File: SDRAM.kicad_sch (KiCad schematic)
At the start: 24 parts, among them J1 Micro_SD_Card_Det_Hirose_DM3AT, U1 W25Q128JVS, U2 IS42S16160J-7TL, U5 W25N01GVZEIG, U7 CAT24C128

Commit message: Looks like FPC should be changed to XF2M-4015-1A
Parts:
- C1, C18, C2, C20, C21, C22, C29, C3, C36, C37, C38: JLCPCB Part # (none) -> C307331
- J1: JLCPCB Part # (none) -> C114218
- R1, R10, R2, R7, R8, R9: JLCPCB Part # (none) -> C25744
- R5, R6: JLCPCB Part # (none) -> C25879
- U2: JLCPCB Part # (none) -> C412833
- U7: JLCPCB Part # (none) -> C6482
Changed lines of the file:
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@@
 			)
 		)
+		(property "JLCPCB Part #" "C307331"
+			(at 224.79 46.99 0)
+			(effects
+				(font
+					(size 1.27 1.27)
+				)
+				(hide yes)
+			)
+		)
 		(pin "1"
 		)
@@
 			)
 		)
+		(property "JLCPCB Part #" "C307331"
+			(at 265.43 46.99 0)
+			(effects
+				(font
+					(size 1.27 1.27)
+				)
+				(hide yes)
+			)
+		)
 		(pin "1"
 		)
@@
 			)
 		)
+		(property "JLCPCB Part #" "C6482"
+			(at 146.05 54.61 0)
+			(effects
+				(font
+					(size 1.27 1.27)
+				)
+				(hide yes)
+			)
+		)
 		(pin "6"
 		)
@@
 			)
 		)
+		(property "JLCPCB Part #" "C25879"
+			(at 161.29 48.26 0)
+			(effects
+				(font
+					(size 1.27 1.27)
+				)
+				(hide yes)
+			)
+		)
 		(pin "1"
 		)
@@
 			)
 		)
+		(property "JLCPCB Part #" "C307331"
+			(at 99.06 50.8 0)
+			(effects
+				(font
+					(size 1.27 1.27)
+				)
+				(hide yes)
+			)
+		)
 		(pin "1"
 		)
@@
 			)
 		)
+		(property "JLCPCB Part #" "C307331"
+			(at 245.11 46.99 0)
+			(effects
+				(font
+					(size 1.27 1.27)
+				)
+				(hide yes)
+			)
+		)
 		(pin "1"
 		)
@@
 			)
 		)
+		(property "JLCPCB Part #" "C25744"
+			(at 34.29 69.85 0)
+			(effects
+				(font
+					(size 1.27 1.27)
+				)
+				(hide yes)
+			)
+		)
 		(pin "1"
 		)
@@
 			)
 		)
+		(property "JLCPCB Part #" "C25744"
+			(at 34.29 38.1 0)
+			(effects
+				(font
+					(size 1.27 1.27)
+				)
+				(hide yes)
+			)
+		)
 		(pin "1"
 		)
@@
 			)
 		)
+		(property "JLCPCB Part #" "C307331"
+			(at 149.86 137.16 0)
+			(effects
+				(font
+					(size 1.27 1.27)
+				)
+				(hide yes)
+			)
+		)
 		(pin "1"
 		)
@@
 			)
 		)
+		(property "JLCPCB Part #" "C307331"
+			(at 255.27 46.99 0)
+			(effects
+				(font
+					(size 1.27 1.27)
+				)
+				(hide yes)
+			)
+		)
 		(pin "1"
 		)
@@
 			)
 		)
+		(property "JLCPCB Part #" "C307331"
+			(at 125.73 53.34 0)
+			(effects
+				(font
+					(size 1.27 1.27)
+				)
+				(hide yes)
+			)
+		)
 		(pin "1"
 		)
@@
 			)
 		)
+		(property "JLCPCB Part #" "C25744"
+			(at 25.4 38.1 0)
+			(effects
+				(font
+					(size 1.27 1.27)
+				)
+				(hide yes)
+			)
+		)
 		(pin "1"
 		)
@@
 			)
 		)
+		(property "JLCPCB Part #" "C307331"
+			(at 214.63 46.99 0)
+			(effects
+				(font
+					(size 1.27 1.27)
+				)
+				(hide yes)
+			)
+		)
 		(pin "1"
 		)
@@
 			)
 		)
+		(property "JLCPCB Part #" "C114218"
+			(at 73.66 53.34 0)
+			(effects
+				(font
+					(size 1.27 1.27)
+				)
+				(hide yes)
+			)
+		)
 		(pin "9"
 		)
@@
 			)
 		)
+		(property "JLCPCB Part #" "C307331"
+			(at 234.95 46.99 0)
+			(effects
+				(font
+					(size 1.27 1.27)
+				)
+				(hide yes)
+			)
+		)
 		(pin "1"
 		)
@@
 			)
 		)
+		(property "JLCPCB Part #" "C412833"
+			(at 240.03 104.14 0)
+			(effects
+				(font
+					(size 1.27 1.27)
+				)
+				(hide yes)
+			)
+		)
 		(pin "48"
 		)
@@
 			)
 		)
+		(property "JLCPCB Part #" "C25744"
+			(at 16.51 38.1 0)
+			(effects
+				(font
+					(size 1.27 1.27)
+				)
+				(hide yes)
+			)
+		)
 		(pin "1"
 		)
@@
 			)
 		)
+		(property "JLCPCB Part #" "C25744"
+			(at 128.27 137.16 0)
+			(effects
+				(font
+					(size 1.27 1.27)
+				)
+				(hide yes)
+			)
+		)
 		(pin "2"
 		)
@@
 			)
 		)
+		(property "JLCPCB Part #" "C25744"
+			(at 46.99 135.89 0)
+			(effects
+				(font
+					(size 1.27 1.27)
+				)
+				(hide yes)
+			)
+		)
 		(pin "2"
 		)
@@
 			)
 		)
+		(property "JLCPCB Part #" "C307331"
+			(at 68.58 135.89 0)
+			(effects
+				(font
+					(size 1.27 1.27)
+				)
+				(hide yes)
+			)
+		)
 		(pin "1"
 		)
@@
 			)
 		)
+		(property "JLCPCB Part #" "C25879"
+			(at 168.91 48.26 0)
+			(effects
+				(font
+					(size 1.27 1.27)
+				)
+				(hide yes)
+			)
+		)
 		(pin "1"
 		)
@@
 			)
 		)
+		(property "JLCPCB Part #" ""
+			(at 139.7 151.13 0)
+			(effects
+				(font
+					(size 1.27 1.27)
+				)
+				(hide yes)
+			)
+		)
 		(pin "8"
 		)
@@
 			)
 		)
+		(property "JLCPCB Part #" ""
+			(at 58.42 149.86 0)
+			(effects
+				(font
+					(size 1.27 1.27)
+				)
+				(hide yes)
+			)
+		)
 		(pin "8"
 		)
@@
 			(at 204.47 46.99 0)
 			(effects
+				(font
+					(size 1.27 1.27)
+				)
+				(hide yes)
+			)
+		)
+		(property "JLCPCB Part #" "C307331"
+			(at 204.47 46.99 0)
+			(effects

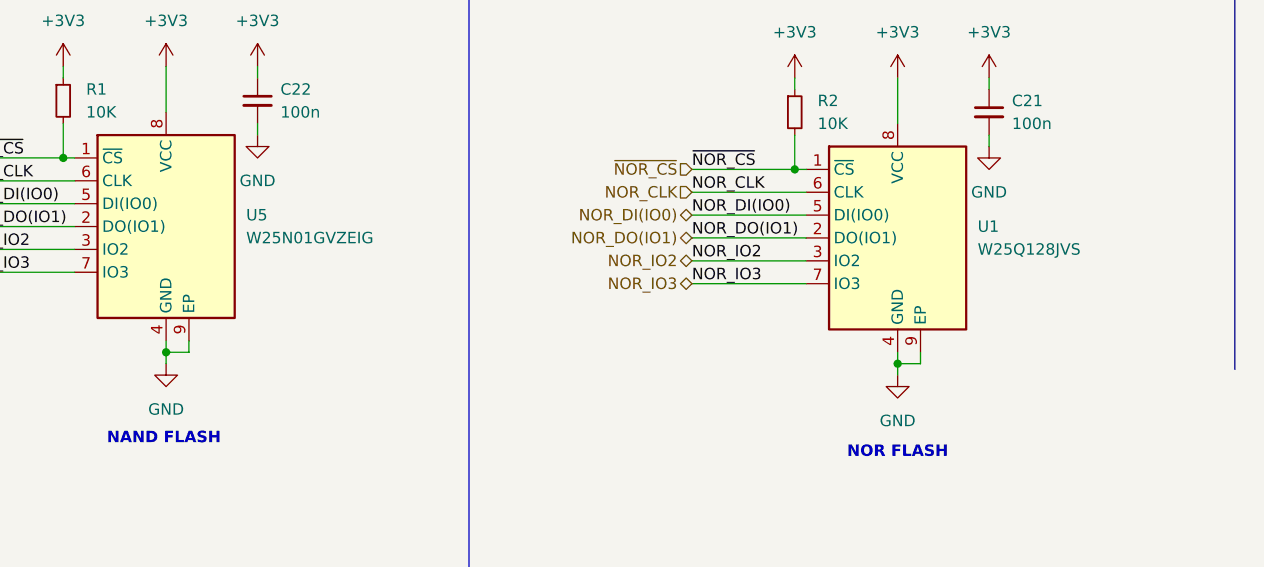
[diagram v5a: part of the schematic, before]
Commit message: Changed the FPC footprint and uart, added RTC battery connector
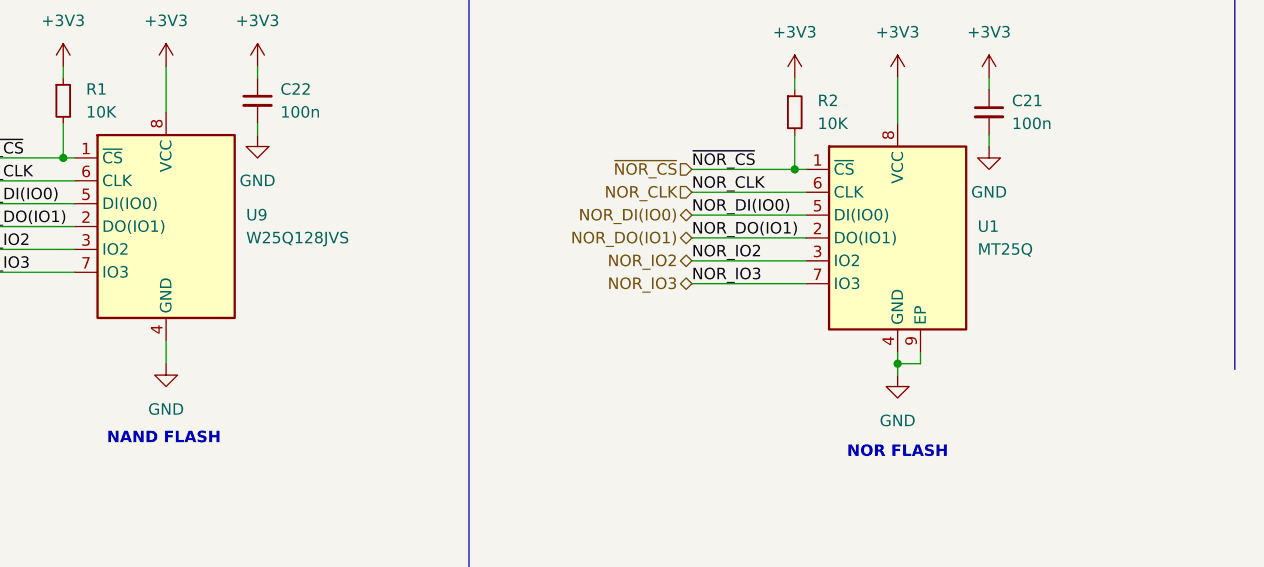
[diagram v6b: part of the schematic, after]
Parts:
- removed U5: W25N01GVZEIG, Package_SON:WSON-8-1EP_6x5mm_P1.27mm_EP3.4x4.3mm, symbol Memory_Flash:W25Q32JVZP
- added U9: W25Q128JVS, Package_SO:SOIC-8_5.23x5.23mm_P1.27mm, symbol Memory_Flash:W25Q128JVS
- U1: value W25Q128JVS -> MT25Q; JLCPCB Part # (none) -> C2061007
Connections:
- net +3V3: now also U9.8 (VCC)
- net GND: now also U9.4 (GND)
- net NAND_CLK: now also U9.6 (CLK)
- net NAND_DI(IO0): now also U9.5 (DI(IO0))
- net NAND_DO(IO1): now also U9.2 (DO(IO1))
- net NAND_IO2: now also U9.3 (IO2)
- net NAND_IO3: now also U9.7 (IO3)
- net ~{NAND_CS}: now also U9.1 (~{CS})

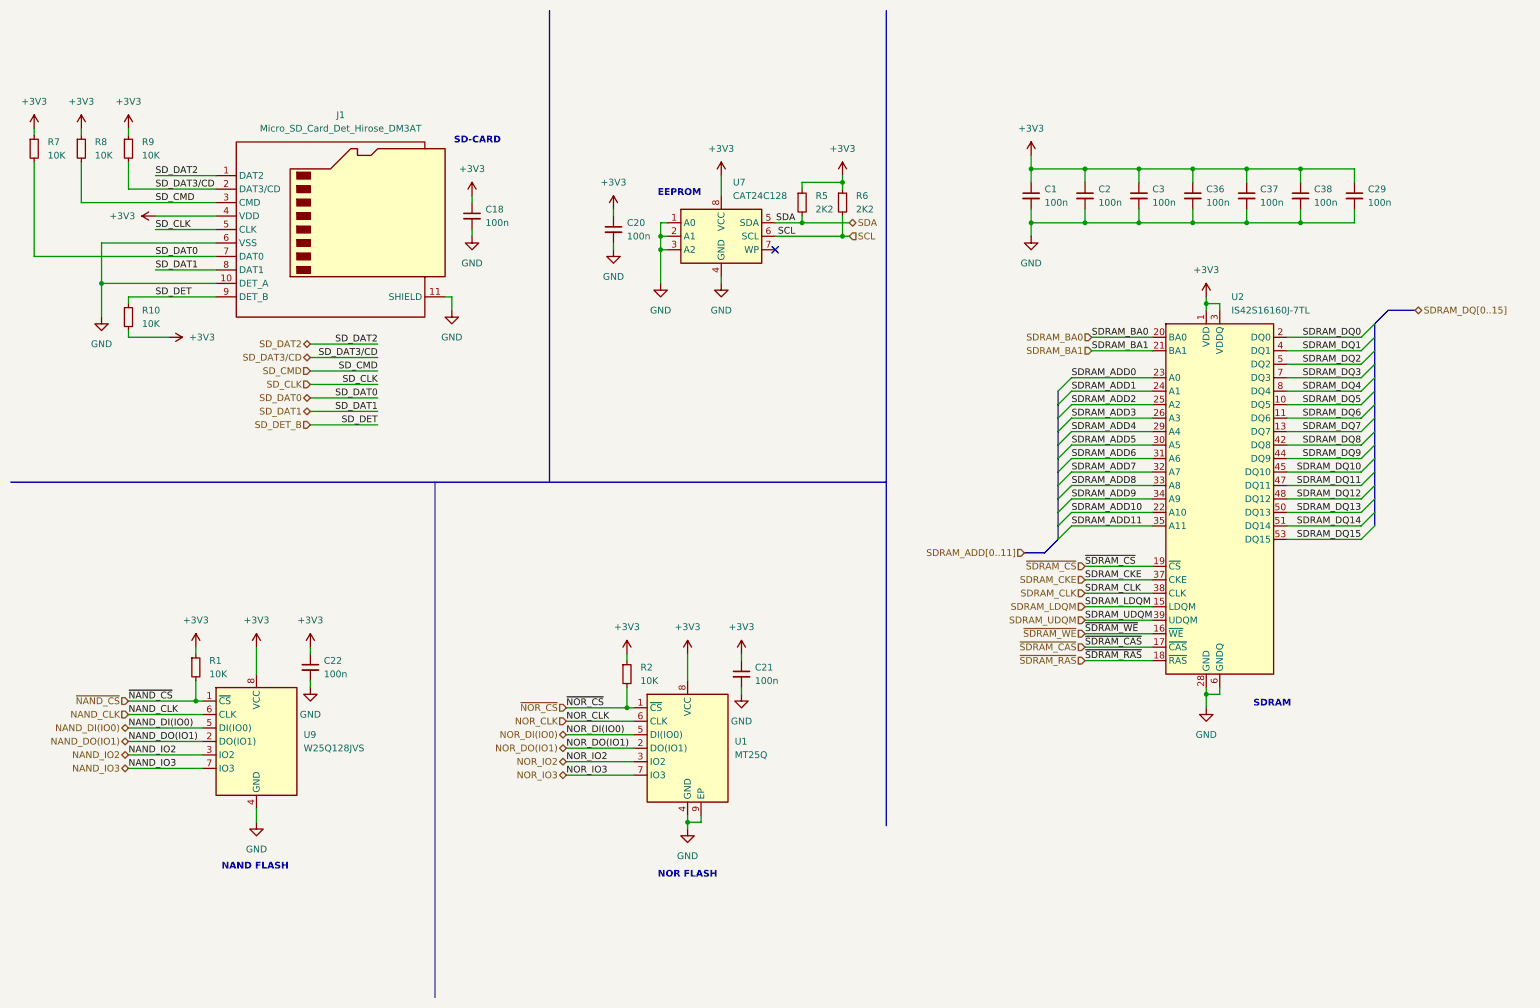
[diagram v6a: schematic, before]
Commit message: All clear (need to verify). LCD backlight driver left untracked
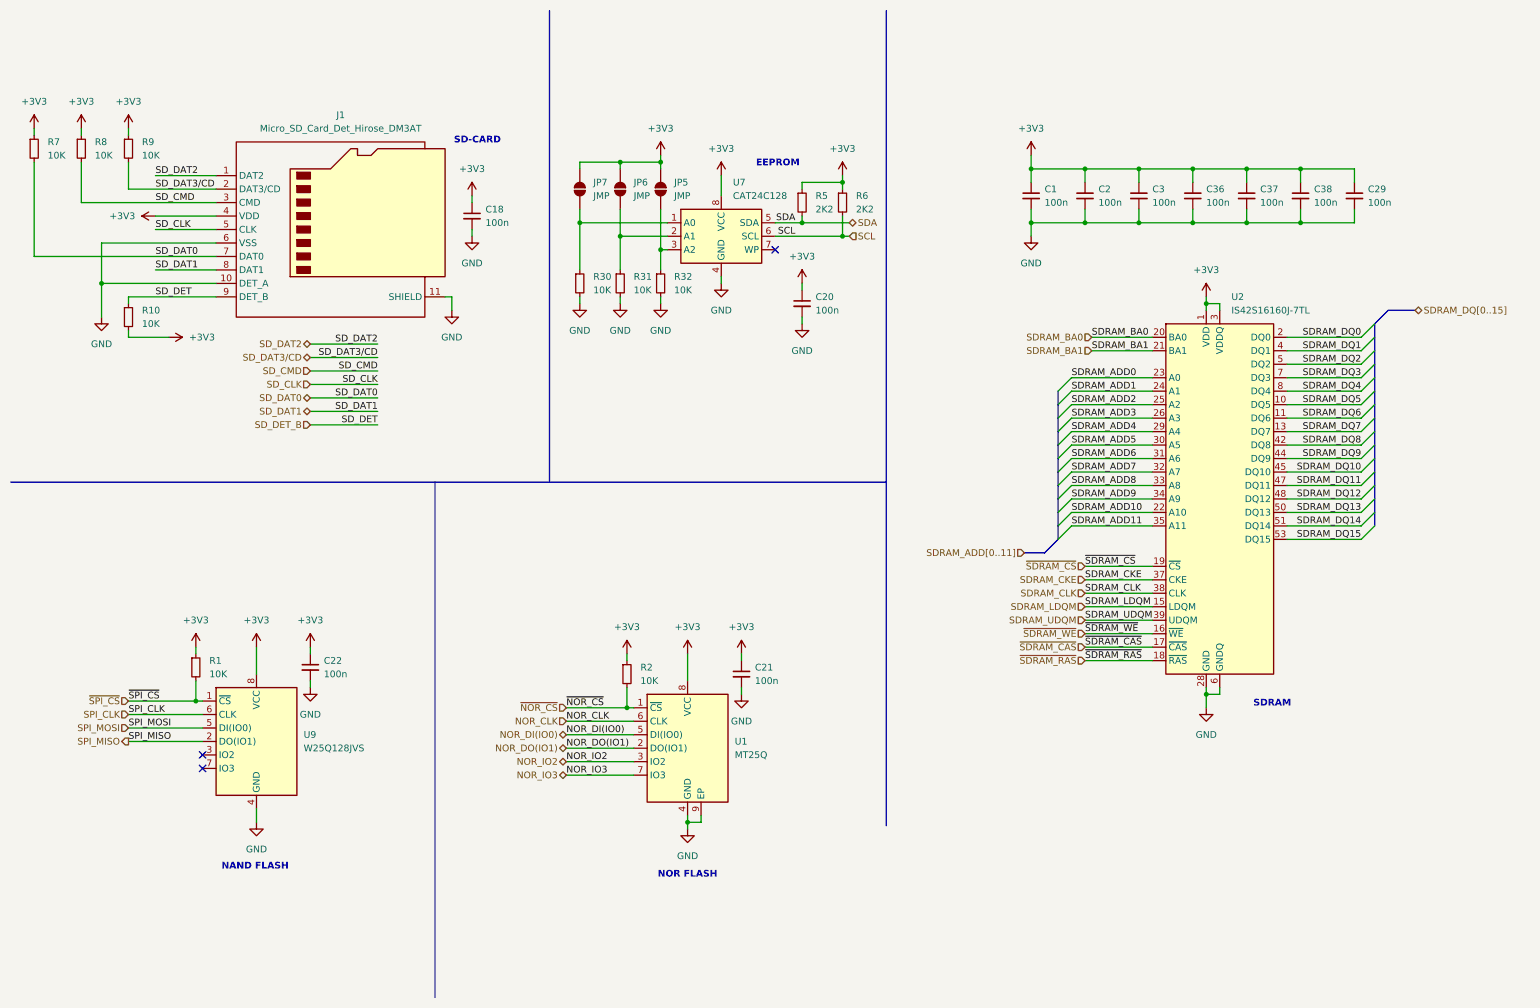
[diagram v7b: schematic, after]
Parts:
- added JP5, JP6, JP7: JMP, Jumper:SolderJumper-2_P1.3mm_Open_RoundedPad1.0x1.5mm, symbol Jumper:SolderJumper_2_Open
- added R30, R31, R32: 10K, Resistor_SMD:R_0402_1005Metric, symbol Device:R_Small
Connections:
- net +3V3: now also JP5.2 (B), JP6.2 (B), JP7.2 (B)
- net GND: now also R30.2, R31.2, R32.2; no longer U7.1 (A0), U7.2 (A1), U7.3 (A2)
- net NAND_CLK renamed SPI_CLK
- net NAND_DI(IO0) renamed SPI_MOSI
- net NAND_DO(IO1) renamed SPI_MISO
- net NAND_IO2: no longer names the net of U9.3 (IO2)
- net NAND_IO3: no longer names the net of U9.7 (IO3)
- net ~{NAND_CS} renamed ~{SPI_CS}
- new net: JP6.1 (A), R31.1, U7.2 (A1)
- new net: JP7.1 (A), R30.1, U7.1 (A0)
- new net: JP5.1 (A), R32.1, U7.3 (A2)
- no-connect marks 1 -> 3
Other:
- moved on the sheet: C20
